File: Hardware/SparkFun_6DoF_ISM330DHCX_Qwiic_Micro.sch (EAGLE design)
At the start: 26 parts, among them J1 Qwiic Right Angle, U1 ISM330DHCX

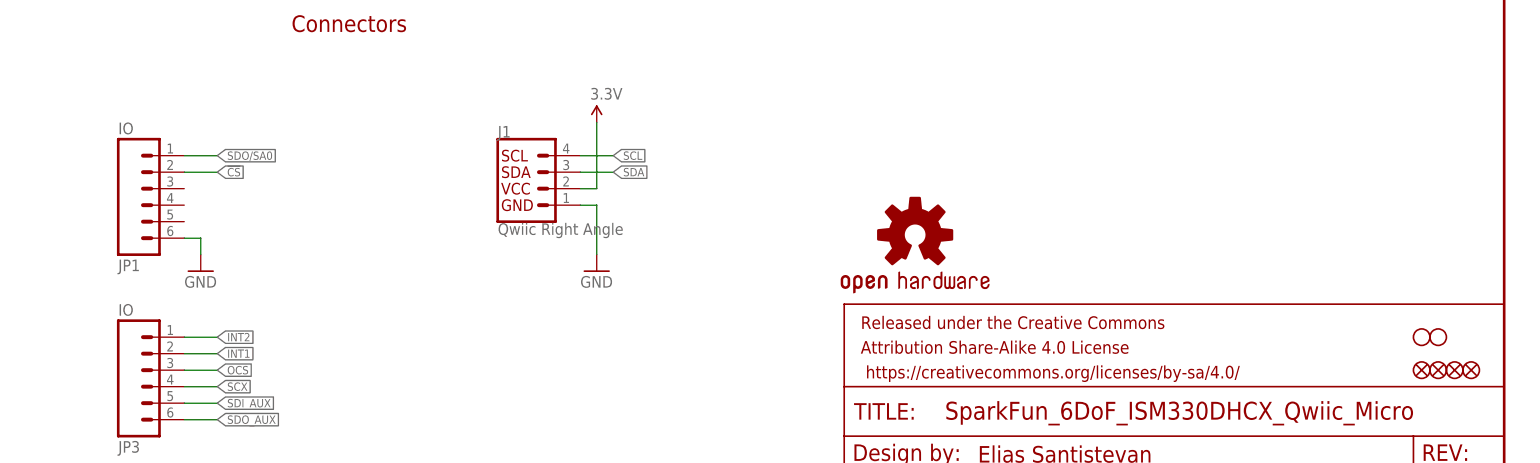
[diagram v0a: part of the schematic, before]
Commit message: Adds a save point for Qwiic Micro - Revert here if removing SPI is not
the way.
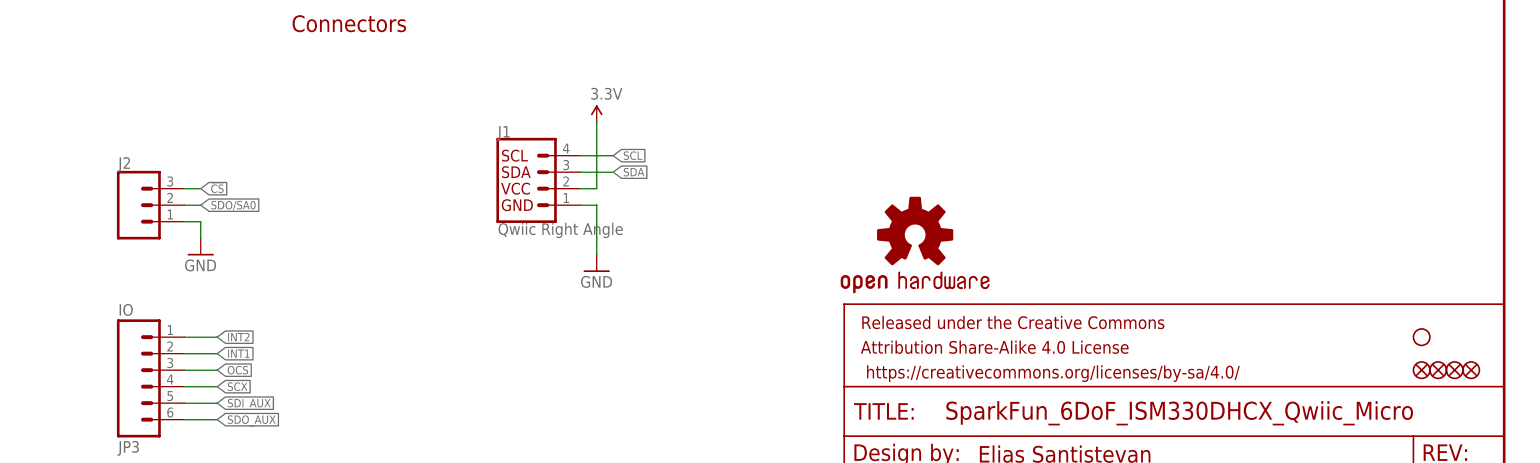
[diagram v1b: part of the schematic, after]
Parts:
- removed JP1: IO, SparkFun-Connectors:CONN_06NO_SILK_NO_POP
- removed STANDOFF2: STAND-OFFTIGHT, SparkFun-Hardware:STAND-OFFTIGHT
- added J2: (no value), SparkFun-Connectors:CONN_031X03_NO_SILK
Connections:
- net !CS!: now also J2.3; no longer JP1.2
- net GND: now also J2.1; no longer JP1.6
- net SDO/SA0: now also J2.2; no longer JP1.1
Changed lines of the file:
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@@
 <part name="LOGO2" library="SparkFun-Aesthetics" deviceset="OSHW-LOGO" device="MINI" value="OSHW-LOGOMINI"/>
 <part name="STANDOFF1" library="SparkFun-Hardware" deviceset="STAND-OFF" device="TIGHT"/>
-<part name="STANDOFF2" library="SparkFun-Hardware" deviceset="STAND-OFF" device="TIGHT"/>
 <part name="R1" library="SparkFun-Resistors" deviceset="2.2KOHM" device="-0402T-1/16W-1%" value="2.2k"/>
 <part name="R2" library="SparkFun-Resistors" deviceset="2.2KOHM" device="-0402T-1/16W-1%" value="2.2k"/>
@@
 <part name="FID1" library="SparkFun-Aesthetics" deviceset="FIDUCIAL" device="UFIDUCIAL" value="FIDUCIALUFIDUCIAL"/>
 <part name="FID2" library="SparkFun-Aesthetics" deviceset="FIDUCIAL" device="UFIDUCIAL" value="FIDUCIALUFIDUCIAL"/>
-<part name="GND11" library="SparkFun-PowerSymbols" deviceset="GND" device=""/>
 <part name="R3" library="SparkFun-Resistors" deviceset="10KOHM" device="-0402T-1/16W-1%" value="10k"/>
 <part name="I2C_PU" library="SparkFun-Jumpers" deviceset="JUMPER-SMT_3_2-NC_TRACE" device="_SILK" package3d_urn="urn:adsk.eagle:package:39289/1" value="S_MODE"/>
-<part name="JP1" library="SparkFun-Connectors" deviceset="CONN_06" device="NO_SILK_NO_POP" value="IO"/>
 <part name="GND1" library="SparkFun-PowerSymbols" deviceset="GND" device=""/>
 <part name="GND2" library="SparkFun-PowerSymbols" deviceset="GND" device=""/>
@@
 <part name="GND3" library="SparkFun-PowerSymbols" deviceset="GND" device=""/>
 <part name="SUPPLY1" library="SparkFun-PowerSymbols" deviceset="3.3V" device=""/>
+<part name="J2" library="SparkFun-Connectors" deviceset="CONN_03" device="1X03_NO_SILK"/>
+<part name="GND8" library="SparkFun-PowerSymbols" deviceset="GND" device=""/>
 </parts>
 <sheets>
@@
 <instance part="LOGO2" gate="G$1" x="158.242" y="46.228" smashed="yes"/>
 <instance part="STANDOFF1" gate="G$1" x="236.22" y="30.48" smashed="yes"/>
-<instance part="STANDOFF2" gate="G$1" x="238.76" y="30.48" smashed="yes"/>
 <instance part="R1" gate="G$1" x="124.46" y="99.06" smashed="yes" rot="R90">
 <attribute name="NAME" x="122.9614" y="95.25" size="1.778" layer="95" font="vector" rot="R90"/>
@@
 <instance part="FID1" gate="G$1" x="236.22" y="25.4" smashed="yes"/>
 <instance part="FID2" gate="G$1" x="238.76" y="25.4" smashed="yes"/>
-<instance part="GND11" gate="1" x="48.26" y="40.64" smashed="yes">
-<attribute name="VALUE" x="45.72" y="38.1" size="1.778" layer="96" font="vector"/>
-</instance>
 <instance part="R3" gate="G$1" x="78.74" y="152.4" smashed="yes" rot="R90">
 <attribute name="NAME" x="77.2414" y="148.59" size="1.778" layer="95" font="vector" rot="R90"/>
@@
 <instance part="I2C_PU" gate="G$1" x="132.08" y="106.68" smashed="yes" rot="MR270">
 <attribute name="NAME" x="127" y="103.759" size="1.778" layer="95" font="vector" rot="MR180"/>
-</instance>
-<instance part="JP1" gate="G$1" x="40.64" y="53.34" smashed="yes" rot="MR180">
-<attribute name="VALUE" x="35.56" y="63.5" size="1.778" layer="96" font="vector" rot="MR180"/>
-<attribute name="NAME" x="35.56" y="42.418" size="1.778" layer="95" font="vector" rot="MR180"/>
 </instance>
 <instance part="GND1" gate="1" x="208.28" y="99.06" smashed="yes">
@@
 <instance part="SUPPLY1" gate="G$1" x="109.22" y="63.5" smashed="yes">
 <attribute name="VALUE" x="108.204" y="67.056" size="1.778" layer="96" font="vector"/>
+</instance>
+<instance part="J2" gate="J$1" x="38.1" y="50.8" smashed="yes">
+<attribute name="VALUE" x="35.56" y="43.434" size="1.778" layer="96" font="vector"/>
+<attribute name="NAME" x="35.56" y="56.388" size="1.778" layer="95" font="vector"/>
+</instance>
+<instance part="GND8" gate="1" x="48.26" y="43.18" smashed="yes">
+<attribute name="VALUE" x="45.72" y="40.64" size="1.778" layer="96" font="vector"/>
 </instance>
 </instances>
@@
 </segment>
 <segment>
-<wire x1="45.72" y1="45.72" x2="48.26" y2="45.72" width="0.1524" layer="91"/>
-<pinref part="GND11" gate="1" pin="GND"/>
-<wire x1="48.26" y1="45.72" x2="48.26" y2="43.18" width="0.1524" layer="91"/>
-<pinref part="JP1" gate="G$1" pin="6"/>
-</segment>
-<segment>
 <pinref part="GND10" gate="1" pin="GND"/>
 <pinref part="C4" gate="G$1" pin="2"/>
@@
 <wire x1="109.22" y1="50.8" x2="109.22" y2="43.18" width="0.1524" layer="91"/>
 <pinref part="GND3" gate="1" pin="GND"/>
+</segment>
+<segment>
+<pinref part="J2" gate="J$1" pin="1"/>
+<wire x1="45.72" y1="48.26" x2="48.26" y2="48.26" width="0.1524" layer="91"/>
+<wire x1="48.26" y1="48.26" x2="48.26" y2="45.72" width="0.1524" layer="91"/>
+<pinref part="GND8" gate="1" pin="GND"/>
 </segment>
 </net>
@@
 </segment>
 <segment>
-<wire x1="45.72" y1="55.88" x2="50.8" y2="55.88" width="0.1524" layer="91"/>
-<label x="50.8" y="55.88" size="1.27" layer="95" font="vector" xref="yes"/>
-<pinref part="JP1" gate="G$1" pin="2"/>
+<wire x1="45.72" y1="53.34" x2="48.26" y2="53.34" width="0.1524" layer="91"/>
+<label x="48.26" y="53.34" size="1.27" layer="95" font="vector" xref="yes"/>
+<pinref part="J2" gate="J$1" pin="3"/>
 </segment>
 </net>
@@
 </segment>
 <segment>
-<wire x1="45.72" y1="58.42" x2="50.8" y2="58.42" width="0.1524" layer="91"/>
-<label x="50.8" y="58.42" size="1.27" layer="95" font="vector" xref="yes"/>
-<pinref part="JP1" gate="G$1" pin="1"/>
-</segment>
-</net>
+<wire x1="45.72" y1="50.8" x2="48.26" y2="50.8" width="0.1524" layer="91"/>
+<label x="48.26" y="50.8" size="1.27" layer="95" font="vector" xref="yes"/>
+<pinref part="J2" gate="J$1" pin="2"/>
+</segment>
+</net>

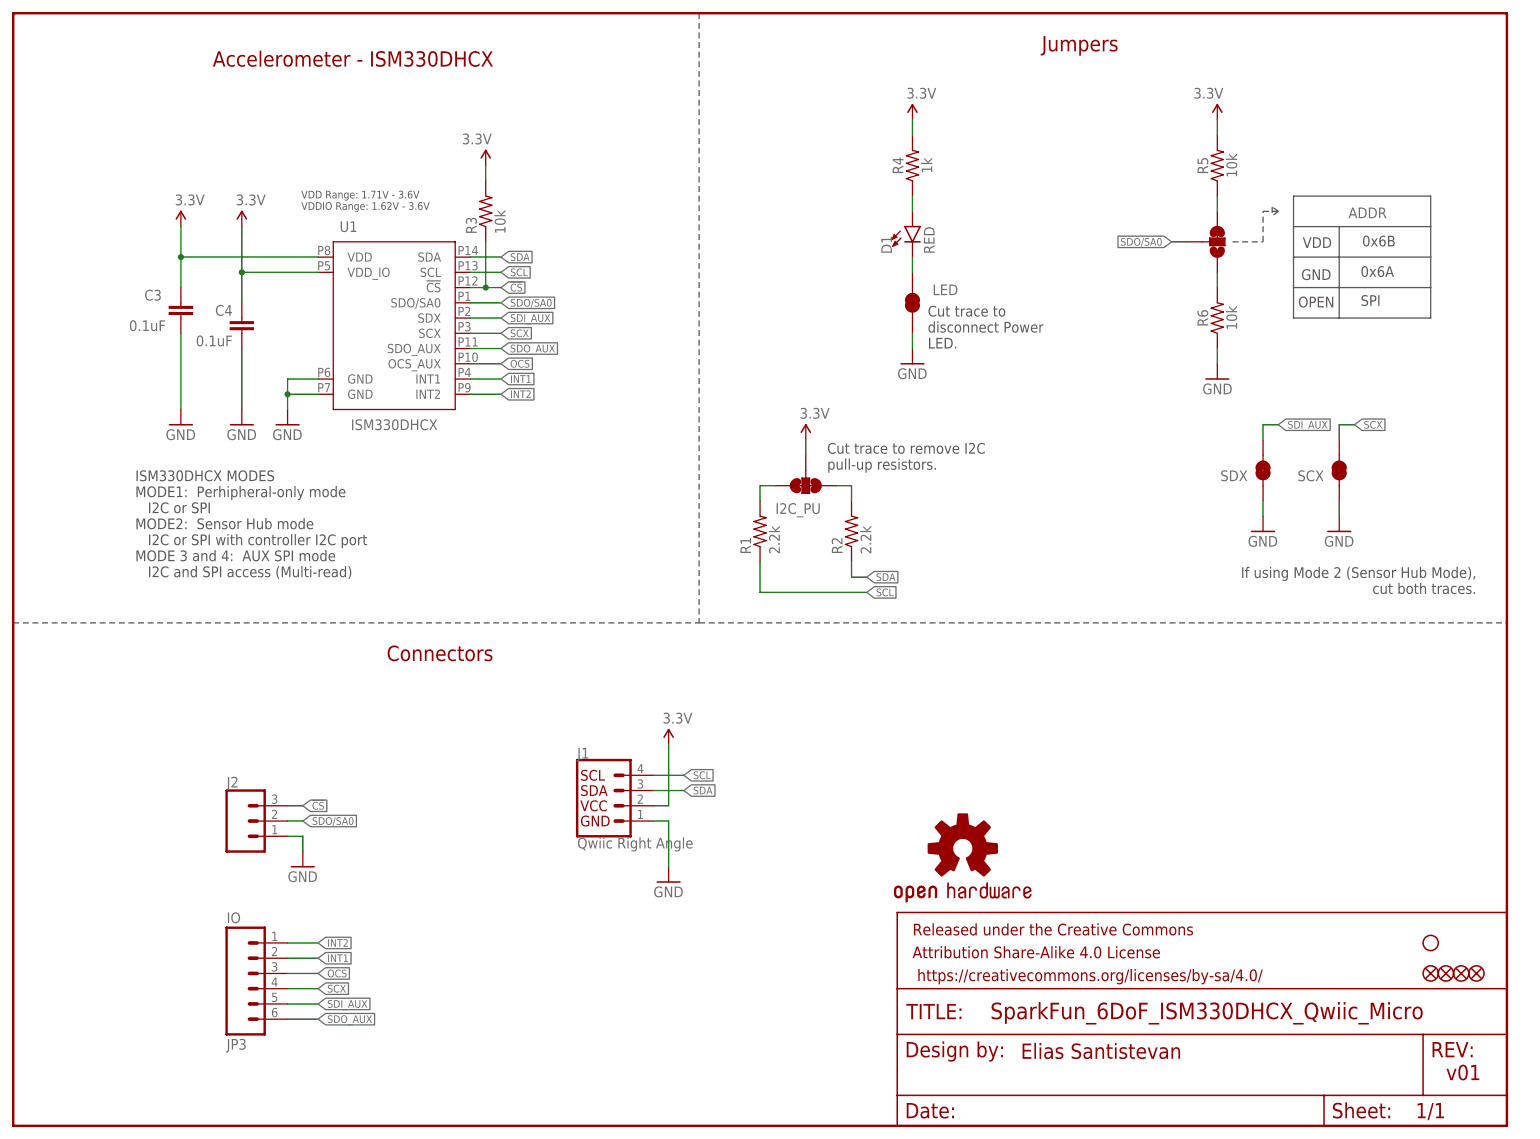
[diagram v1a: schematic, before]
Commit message: Removes Auxiliary pins to make the Qwiic Micro as Micro as possible
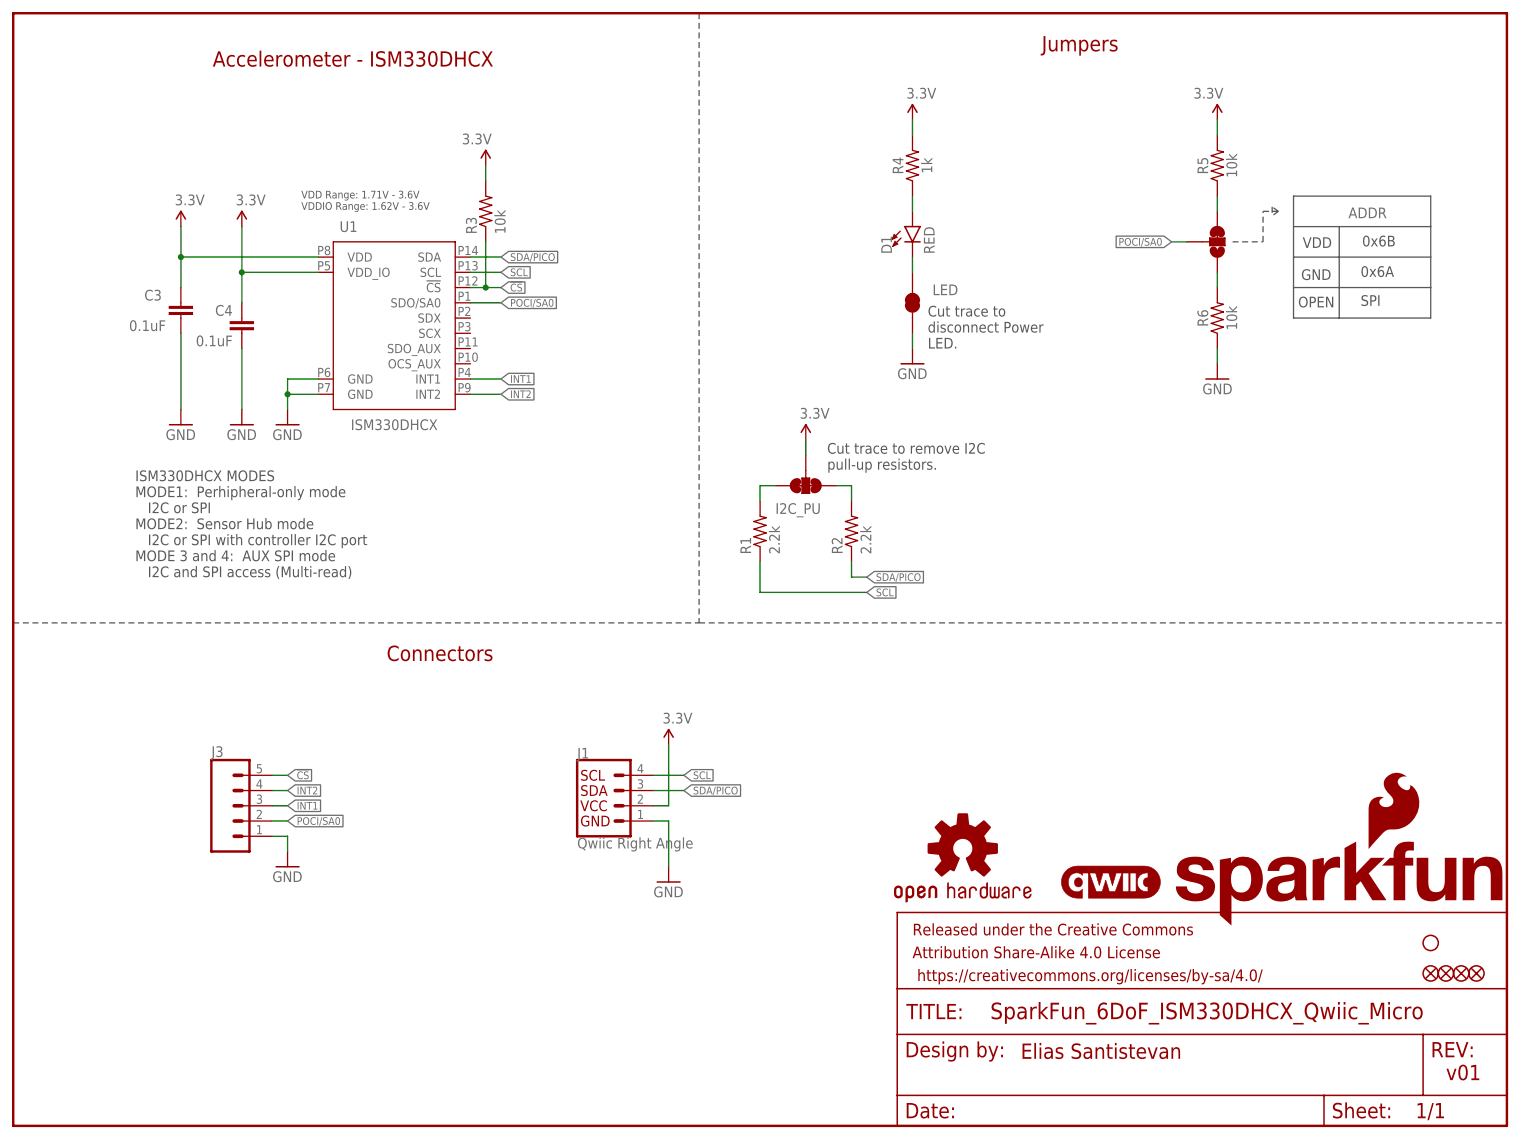
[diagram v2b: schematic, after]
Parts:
- removed J2: (no value), SparkFun-Connectors:CONN_031X03_NO_SILK
- removed JP3: IO, SparkFun-Connectors:CONN_06NO_SILK_NO_POP
- removed SCX, SDX: JUMPER-SMT_2_NC_TRACE_SILK, SparkFun-Jumpers:JUMPER-SMT_2_NC_TRACE_SILK
- added J3: (no value), SparkFun-Connectors:CONN_05NO_SILK
- added LOGO1: QWIIC_LOGO_3MM, SparkFun-Aesthetics:QWIIC_LOGO_3MM
- added LOGO3: SFE_LOGO_NAME_FLAMEBLANK, SparkFun-Aesthetics:SFE_LOGO_NAME_FLAMEBLANK
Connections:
- net SDA renamed SDA/PICO
- removed net OCS: JP3.3, U1.OCS_AUX
- removed net SCX: JP3.4, SCX.2, U1.SCX
- removed net SDI_AUX: JP3.5, SDX.2, U1.SDX
- removed net SDO/SA0: ADDR.2, J2.2, U1.SDO/SA0
- removed net SDO_AUX: JP3.6, U1.SDO_AUX
- new net POCI/SA0: ADDR.2, J3.2, U1.SDO/SA0
- net !CS!: now also J3.5; no longer J2.3
- net GND: now also J3.1; no longer J2.1, SCX.1, SDX.1
- net INT1: now also J3.3; no longer JP3.2
- net INT2: now also J3.4; no longer JP3.1
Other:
- note removed: "If using Mode 2 (Sensor Hub Mode), cut both traces."
